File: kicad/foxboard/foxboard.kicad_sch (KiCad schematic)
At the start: 183 parts, among them J2 USB_C_Receptacle_USB2.0, K1 KEYSW, K10 KEYSW, K11 KEYSW, K12 KEYSW, K13 KEYSW, K14 KEYSW, K15 KEYSW, K16 KEYSW, K17 KEYSW, K18 KEYSW, K19 KEYSW, K2 KEYSW, K20 KEYSW, K21 KEYSW, K22 KEYSW, K23 KEYSW, K24 KEYSW, K25 KEYSW, K26 KEYSW, K27 KEYSW, K28 KEYSW, K29 KEYSW, K3 KEYSW, K30 KEYSW, K31 KEYSW, K32 KEYSW, K33 KEYSW, K34 KEYSW, K35 KEYSW, K36 KEYSW, K37 KEYSW, K38 KEYSW, K39 KEYSW, K4 KEYSW, K40 KEYSW, K41 KEYSW, K42 KEYSW, K43 KEYSW, K44 KEYSW, K45 KEYSW, K46 KEYSW, K47 KEYSW, K48 KEYSW, K49 KEYSW, K5 KEYSW, K50 KEYSW, K51 KEYSW, K52 KEYSW, K53 KEYSW, K54 KEYSW, K55 KEYSW, K56 KEYSW, K57 KEYSW, K58 KEYSW, K59 KEYSW, K6 KEYSW, K60 KEYSW, K61 KEYSW, K62 KEYSW, K63 KEYSW, K64 KEYSW, K65 KEYSW, K66 KEYSW, K67 KEYSW, K68 KEYSW, K69 KEYSW, K7 KEYSW, K70 KEYSW, K71 KEYSW, K72 KEYSW, K73 KEYSW, K74 KEYSW, K75 KEYSW, K76 KEYSW, K77 KEYSW, K78 KEYSW, K79 KEYSW, K8 KEYSW, K80 KEYSW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

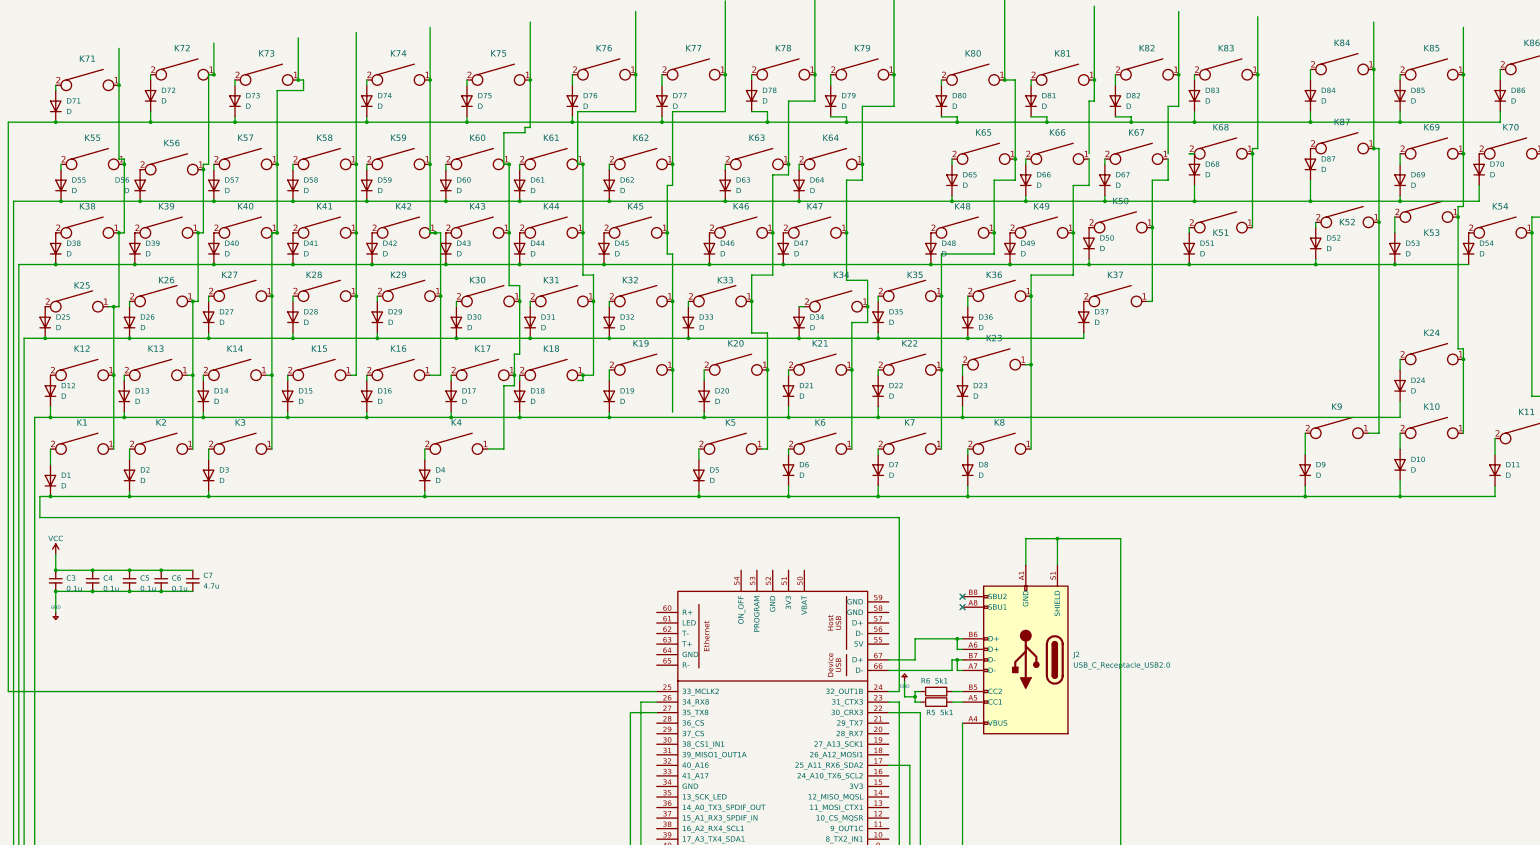
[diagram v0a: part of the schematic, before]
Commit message: add few cols & update eeschema
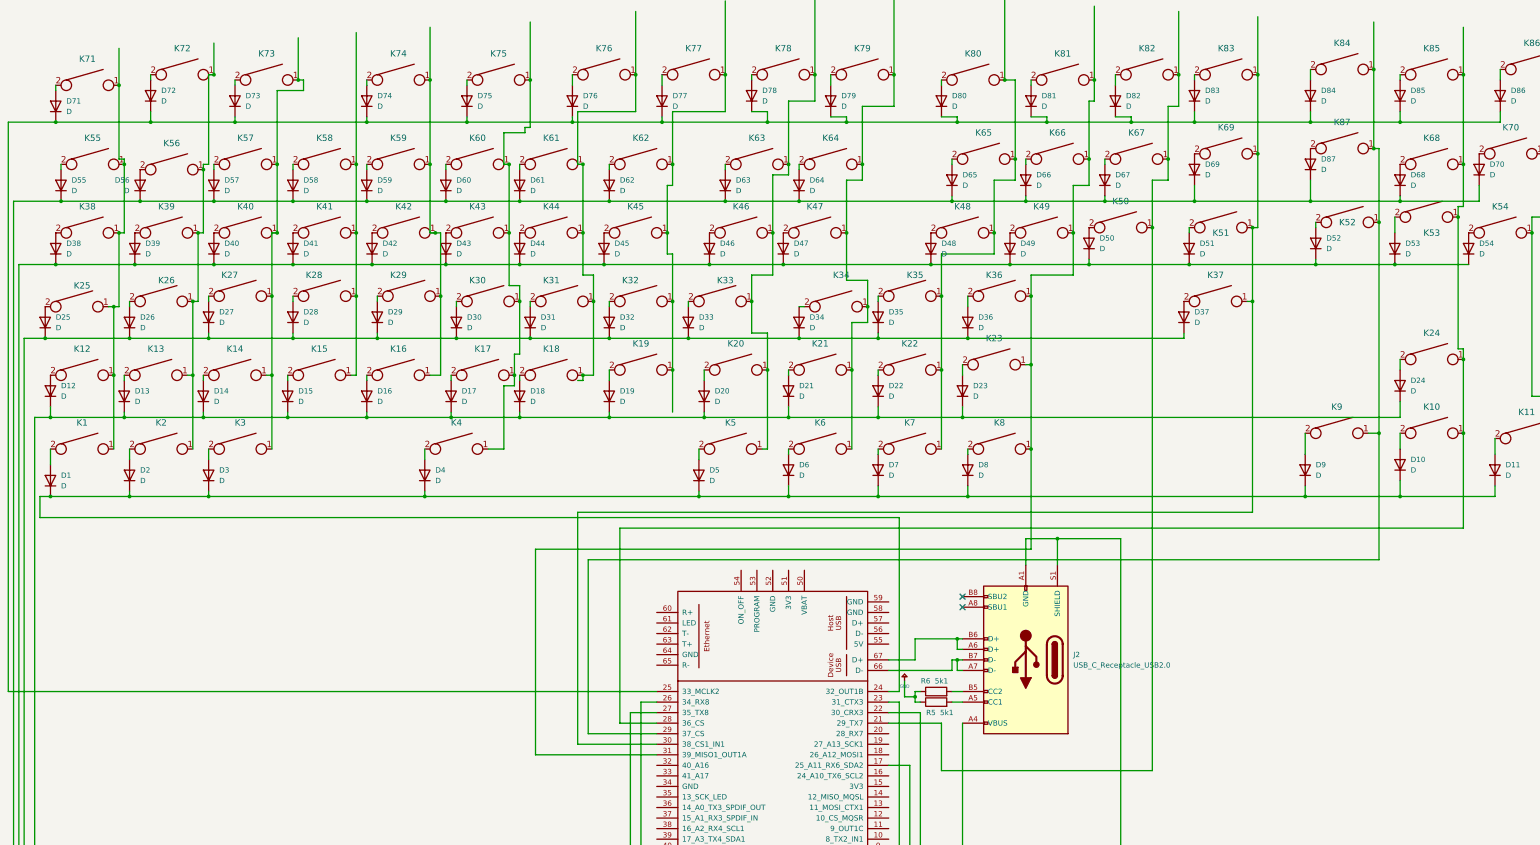
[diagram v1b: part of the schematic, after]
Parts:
- removed C3, C4, C5, C6: 0.1u, Capacitor_SMD:C_0201_0603Metric_Pad0.64x0.40mm_HandSolder, symbol Device:C_Small
- removed C7: 4.7u, Capacitor_SMD:C_0201_0603Metric_Pad0.64x0.40mm_HandSolder, symbol Device:C_Small
- K12, K23: footprint PCM_marbastlib-xp-plate-mx:Plate_MX_SPLIT-RSHIFT -> PCM_marbastlib-mx:SW_MX_1u
- K25: footprint PCM_marbastlib-mx:STAB_MX_2.25u -> PCM_marbastlib-mx:SW_MX_1u
- K37: footprint PCM_marbastlib-mx:STAB_MX_ISO -> PCM_marbastlib-mx:SW_MX_1u
- K69: footprint PCM_marbastlib-mx:STAB_MX_2.75u -> PCM_marbastlib-mx:SW_MX_1u
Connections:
- net at K10.1, K24.1, K53.1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: now also K68.1, U2.28 (36_CS); no longer K69.1
- net at K52.1, K84.1, K87.1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: now also U2.29 (37_CS)
- net at K81.1: now also K23.1, K36.1, K49.1, K66.1, K8.1, U2.31 (39_MISO1_OUT1A)
- net at U2.21 (29_TX7): now also K50.1, K67.1, K82.1
- net at U2.30 (38_CS1_IN1): now also K37.1, K51.1, K69.1, K83.1
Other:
- moved on the sheet: D37, D69, K37, K69

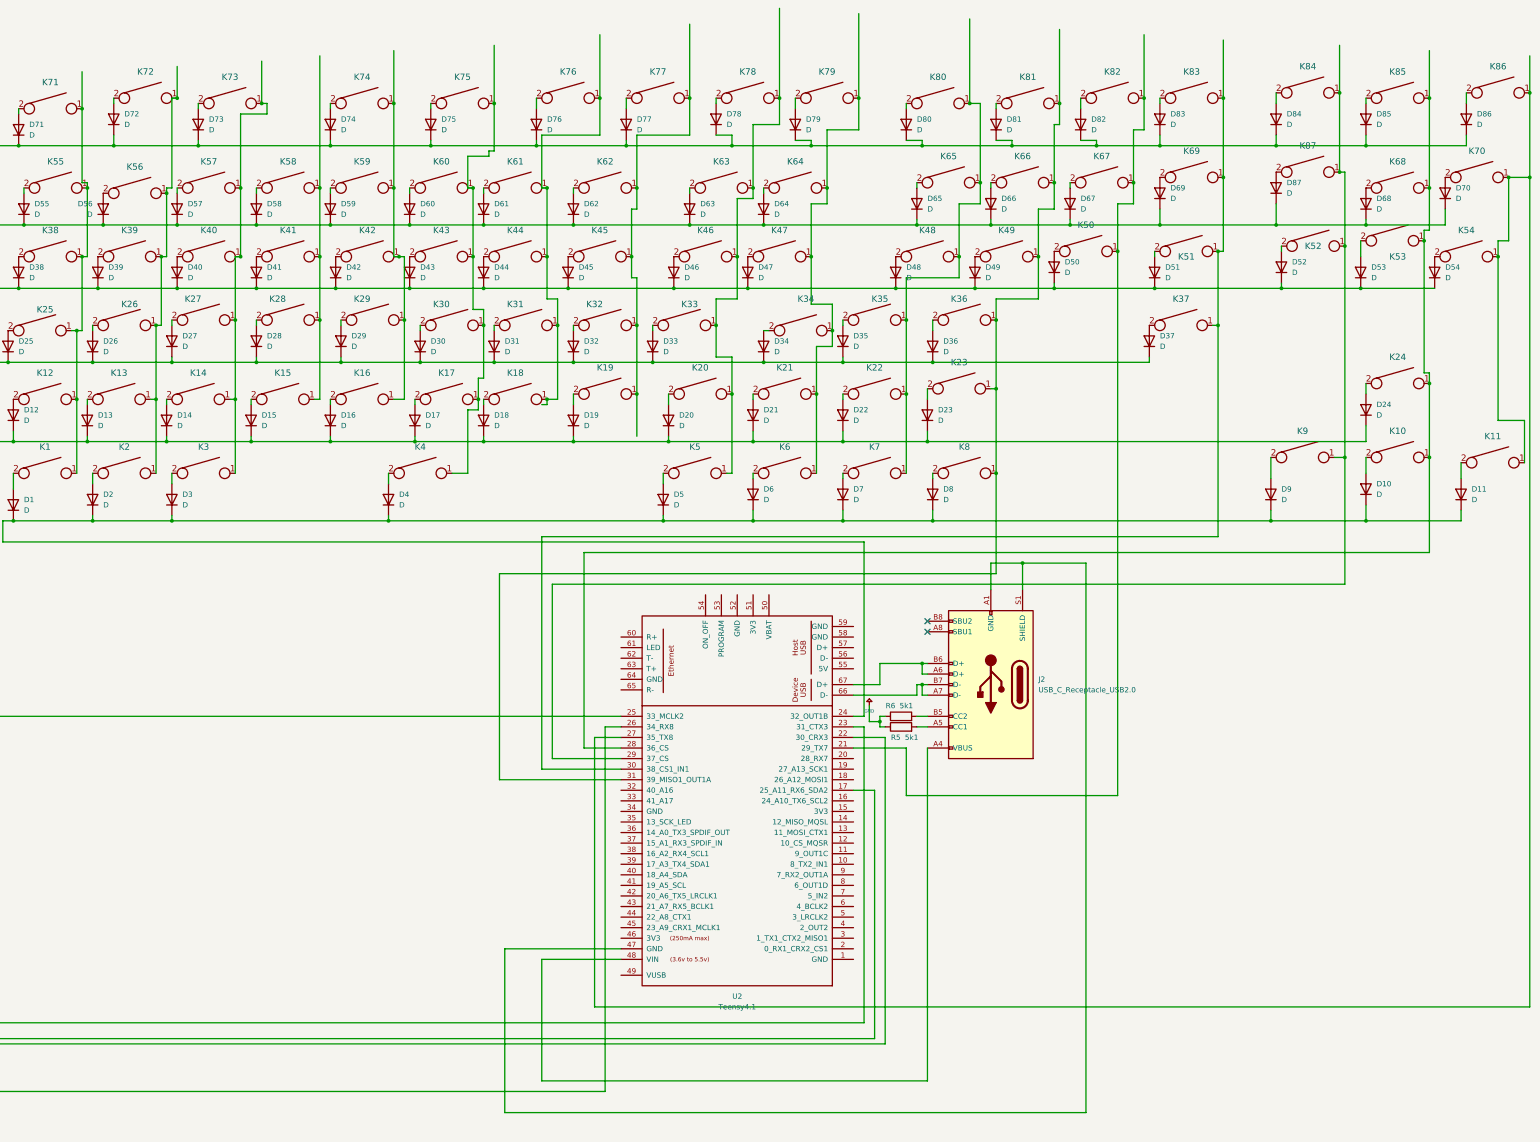
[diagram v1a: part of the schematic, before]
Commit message: add finish cols and usbc & update eeschema
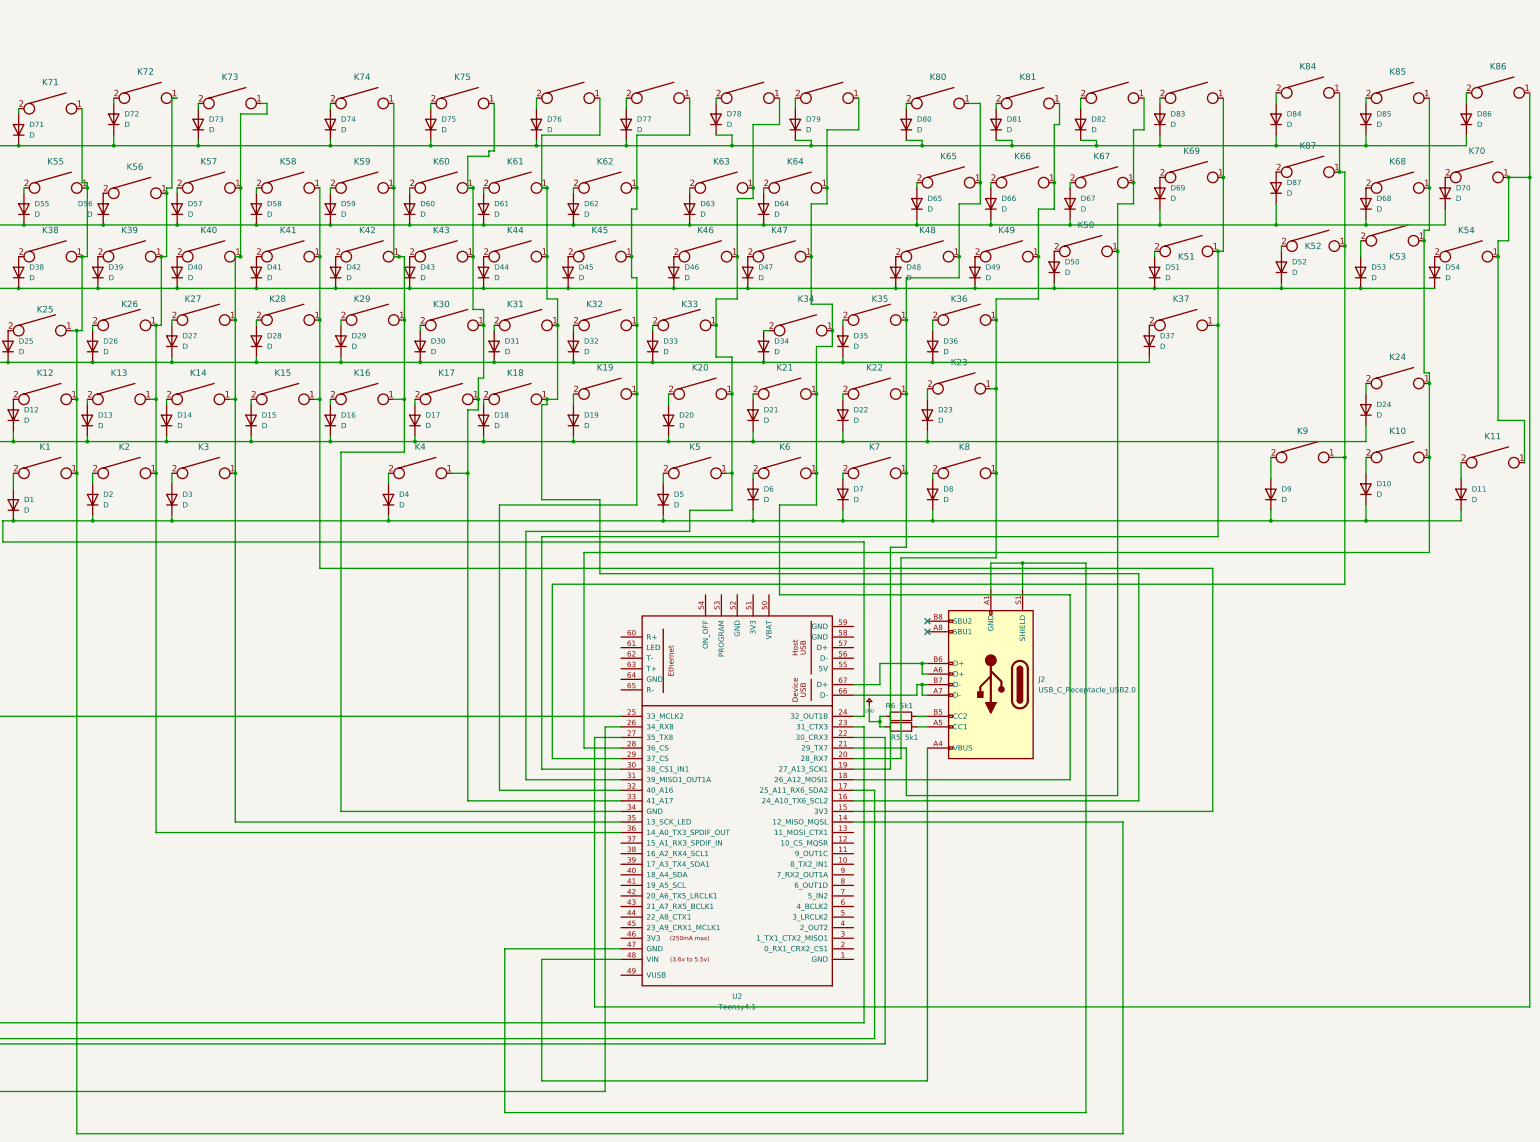
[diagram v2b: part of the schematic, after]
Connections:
- net at K1.1, K12.1, K25.1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: now also U2.14 (12_MISO_MQSL)
- net at K19.1, K32.1, K45.1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: now also U2.32 (40_A16)
- net at K21.1, K34.1, K47.1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: now also U2.18 (26_A12_MOSI1)
- net at K23.1, K36.1, K49.1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: now also U2.20 (28_RX7); no longer U2.31 (39_MISO1_OUT1A)
- net at K14.1, K27.1, K3.1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: now also U2.35 (13_SCK_LED)
- net at U2.15 (3V3): now also K15.1, K28.1, K41.1, K58.1
- net at U2.16 (24_A10_TX6_SCL2): now also K18.1, K31.1, K44.1, K61.1, K76.1
- net at U2.19 (27_A13_SCK1): now also K22.1, K35.1, K48.1, K65.1, K7.1, K80.1
- net at U2.33 (41_A17): now also K17.1, K30.1, K4.1, K43.1, K60.1, K75.1
- net at U2.34 (GND): now also K16.1, K29.1, K42.1, K59.1, K74.1
- net at U2.36 (14_A0_TX3_SPDIF_OUT): now also K13.1, K2.1, K26.1, K39.1, K56.1, K72.1
- net at K20.1, K33.1, K46.1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: now also U2.31 (39_MISO1_OUT1A)

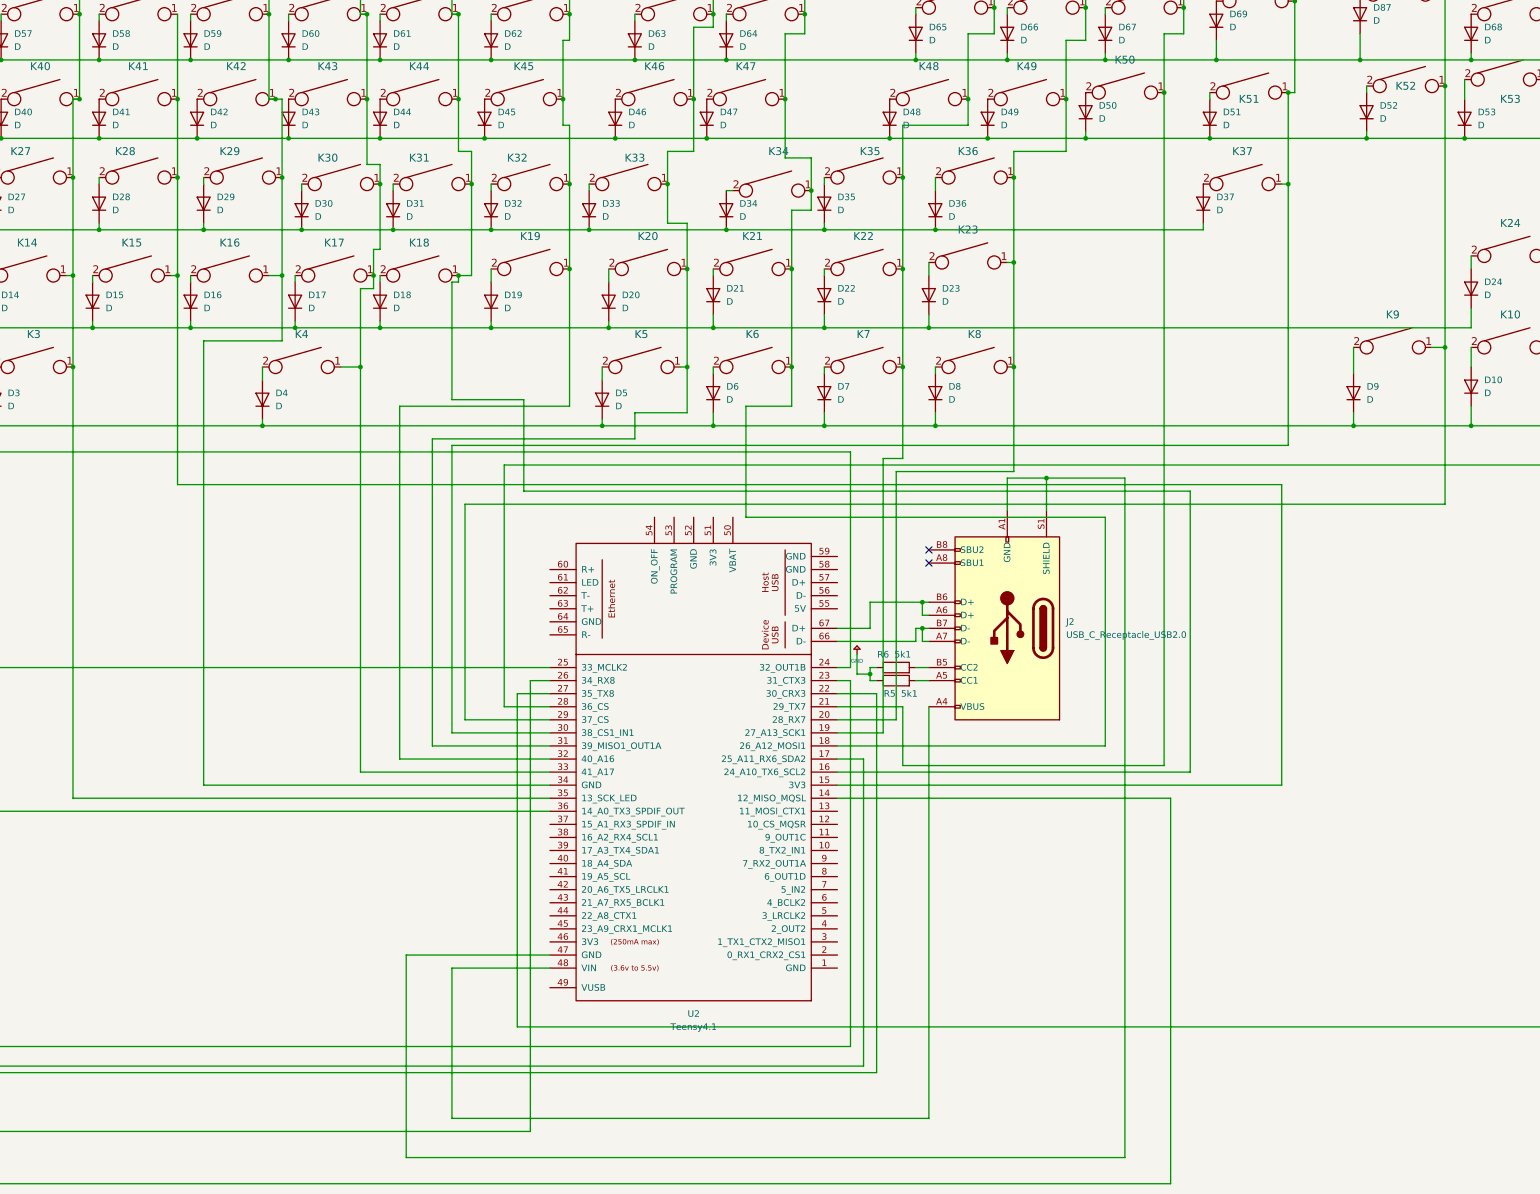
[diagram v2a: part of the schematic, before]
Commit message: Cleaned up the USB-C connector layout and made use of power symbols for schematic clarity
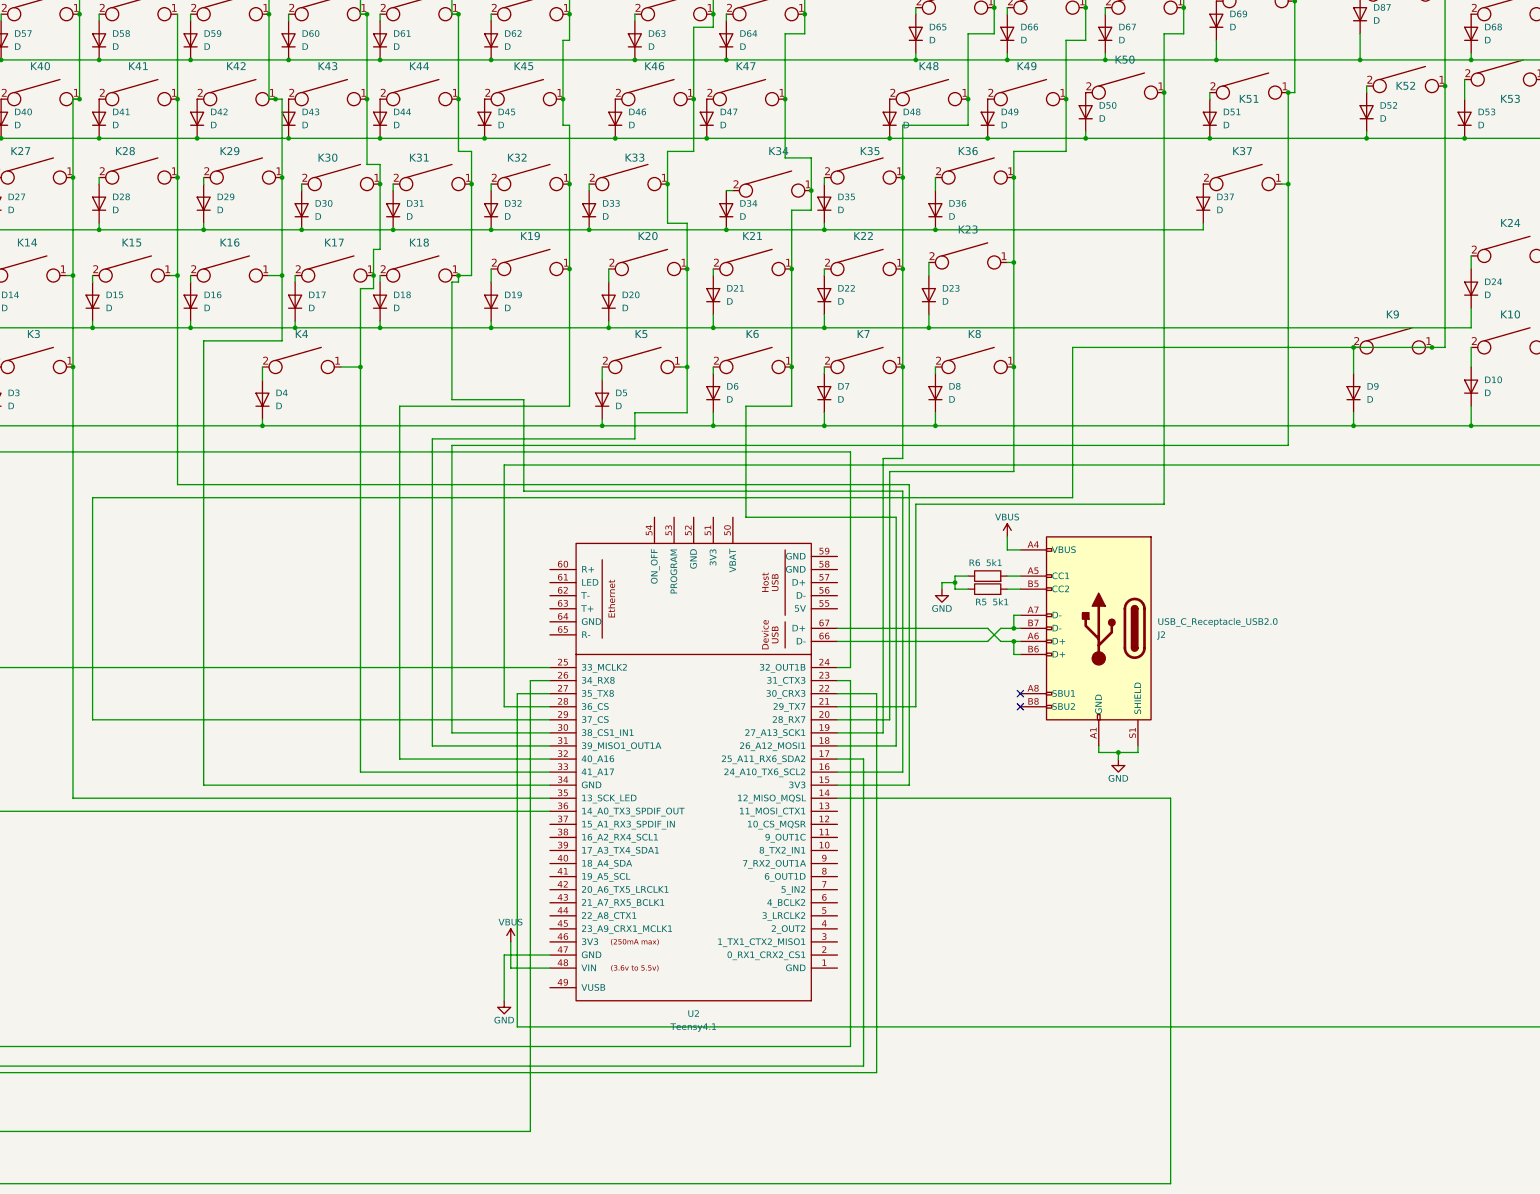
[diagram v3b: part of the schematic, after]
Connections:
- net +5V is gone; now on net GND: R5.1, R6.1
- net at K52.1, K84.1, K87.1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: now also D9.2 (A), K9.2
- net GND: now reaches J2.A1 (GND), J2.A12 (GND), J2.B1 (GND), J2.B12 (GND), J2.S1 (SHIELD), U2.47 (GND)
- net VBUS: now reaches J2.A4 (VBUS), J2.A9 (VBUS), J2.B4 (VBUS), J2.B9 (VBUS), U2.48 (VIN)
- net at J2.A5 (CC1): now also R6.2; no longer R5.2
- net at J2.B5 (CC2): now also R5.2; no longer R6.2
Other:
- moved on the sheet: J2, R5, R6
